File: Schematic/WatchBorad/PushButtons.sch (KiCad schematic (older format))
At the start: 16 parts, among them SW5 SW_Push, SW6 SW_Push, SW7 SW_Push, SW8 SW_Push, SW9 SW_Push, U6 max16054azt+t

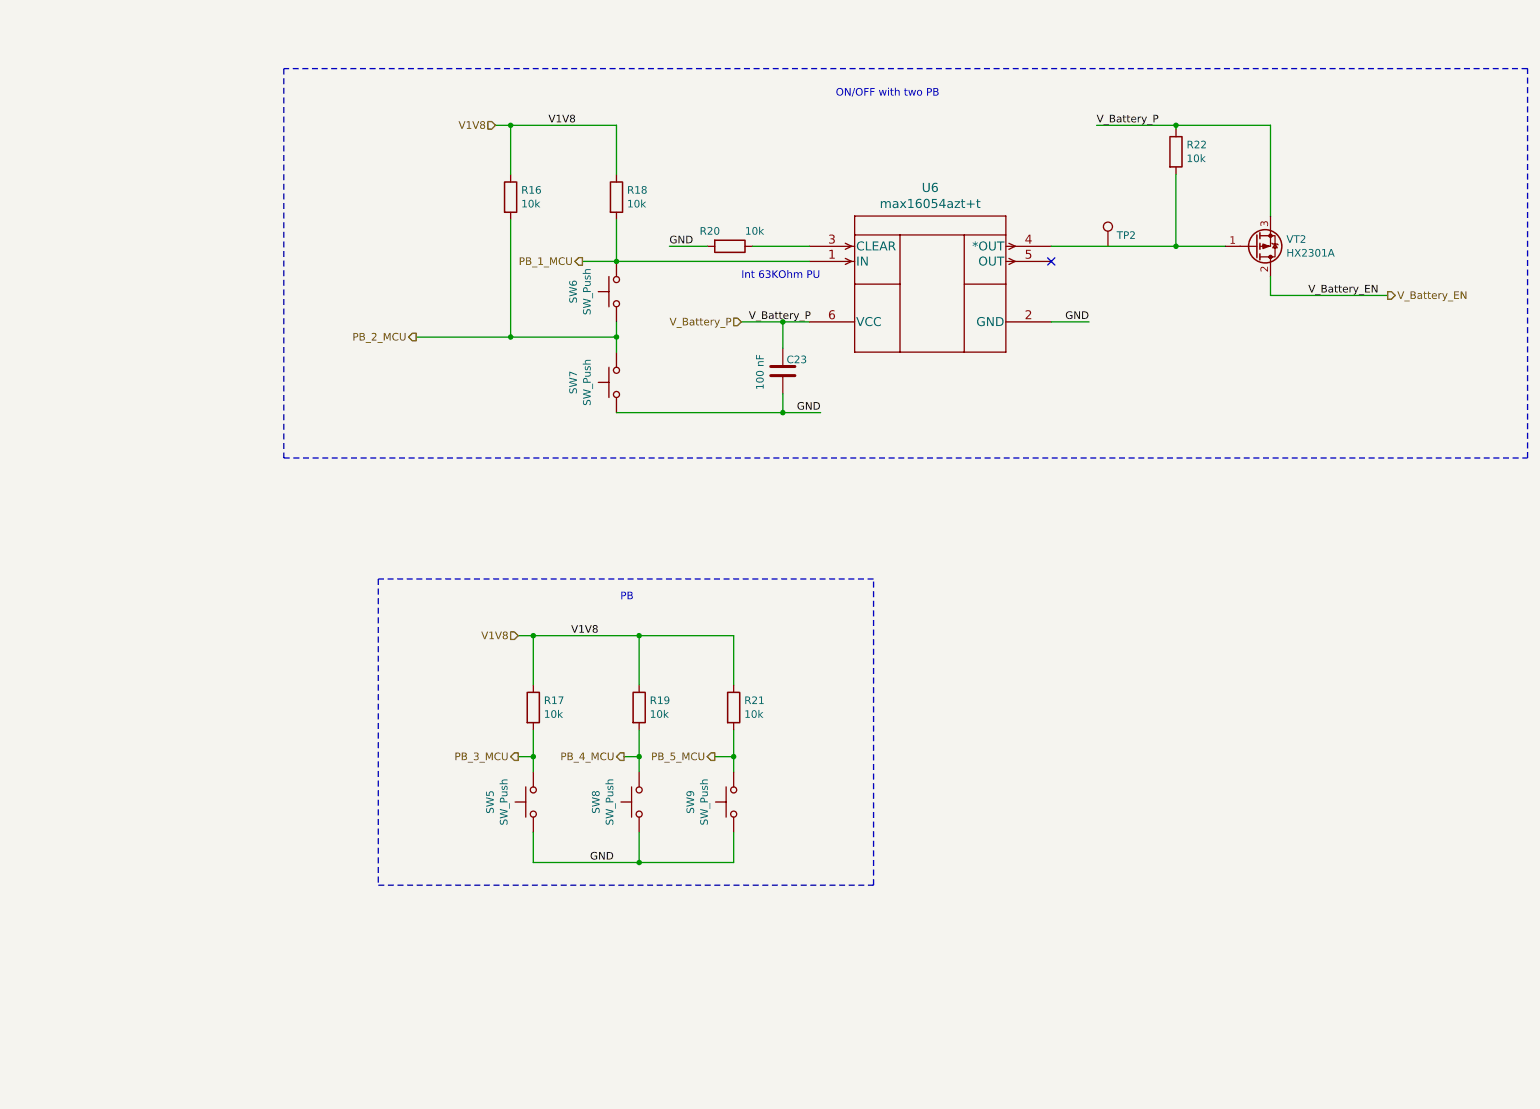
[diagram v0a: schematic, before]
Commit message: Display is replaced, now it has single power supply. One PSU is removed. Circuit PB is modified.
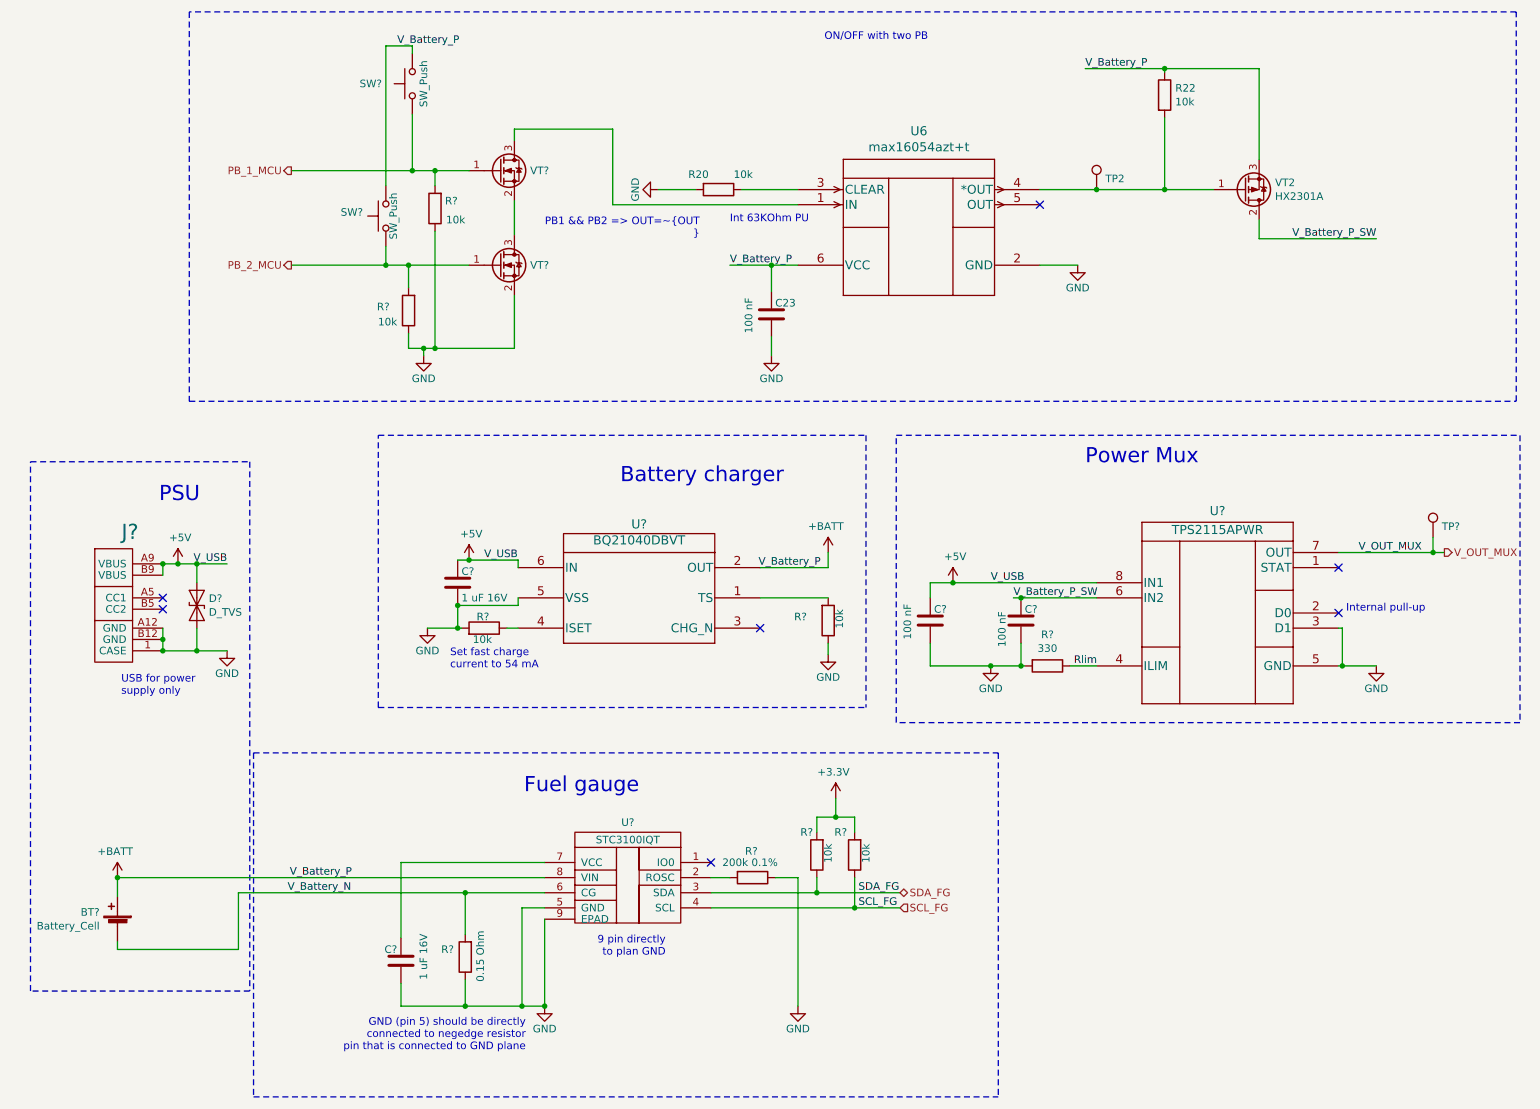
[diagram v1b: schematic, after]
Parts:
- removed R16, R17, R18, R19, R21: 10k, Resistors_SMD:R_0603_HandSoldering, symbol Device:R
- removed SW5, SW6, SW7, SW8, SW9: SW_Push, symbol Switch:SW_Push
- added BT?: Battery_Cell, symbol Device:Battery_Cell
- added C? (x2): 1 uF 16V, Capacitors_SMD:C_0603_HandSoldering, symbol Device:C
- added C? (x2): 100 nF, Capacitors_SMD:C_0603_HandSoldering, symbol Device:C
- added D?: D_TVS, symbol Device:D_TVS
- added J?: TYPE-C-31-M-17, symbol USB_connectors:TYPE-C-31-M-17
- added R? (x6): 10k, Resistors_SMD:R_0603_HandSoldering, symbol Device:R
- added R?: 200k 0.1%, Resistors_SMD:R_0603_HandSoldering, symbol Device:R
- added R?: 0.15 Ohm, Resistors_SMD:R_0603_HandSoldering, symbol Device:R
- added R?: 330, Resistors_SMD:R_0603_HandSoldering, symbol Device:R
- added SW? (x2): SW_Push, symbol Switch:SW_Push
- added TP?: TestPoint, testpoints:testpoint, symbol Connector:TestPoint
- added U?: BQ21040DBVT, TO_SOT_Packages_SMD:SOT-23-6, symbol BatteryManagmentLocal:BQ21040DBVT
- added U?: STC3100IQT, Housings_DFN_QFN:DFN-8-1EP_3x3mm_Pitch0.5mm, symbol BatteryManagmentLocal:STC3100IQT
- added U?: TPS2115APWR, Housings_SSOP:TSSOP-8_4.4x3mm_Pitch0.65mm, symbol PowerMuxes:TPS2115APWR
- added VT? (x2): SL2300, TO_SOT_Packages_SMD:SOT-23, symbol MosfetLocal:SL2300
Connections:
- net GND: now also C?.2, C?.2, C?.2, C?.2, D?.2 (A2), J?.1 (CASE), J?.A12 (GND), J?.B12 (GND), R?.1, R?.1, R?.1, R?.1, R?.1, R?.2, R?.2, U?.3 (D1), U?.5 (GND), U?.5 (GND), U?.5 (VSS), U?.9 (EPAD), VT?.2 (S)
- net PB_1_MCU: now also R?.2, SW?.1, VT?.1 (G); no longer U6.1 (IN)
- net PB_2_MCU: now also R?.2, SW?.1, VT?.1 (G)
- net at R22.2, U6.4 (*OUT), VT2.1 (G): now also TP2.1
- net V_Battery_EN renamed V_Battery_P_SW
- net V_Battery_P_SW: now also C?.1, U?.6 (IN2)
- net V_Battery_P renamed +BATT
- net +BATT: now also BT?.1 (+), SW?.2, SW?.2, U?.2 (OUT), U?.8 (VIN)
- new net: U6.1 (IN), VT?.3 (D)
- new net: R?.2, U?.1 (TS)
- new net: R?.1, U?.4 (ISET)
- new net: R?.2, U?.2 (ROSC)
- new net: C?.1, U?.7 (VCC)
- new net: VT?.2 (S), VT?.3 (D)
- new net +3V3: R?.2, R?.2
- new net +5V: C?.1, C?.1, D?.1 (A1), J?.A9 (VBUS), J?.B9 (VBUS), U?.6 (IN), U?.8 (IN1)
- new net Rlim: R?.1, U?.4 (ILIM)
- new net SCL_FG: R?.1, U?.4 (SCL)
- new net SDA_FG: R?.1, U?.3 (SDA)
- new net V_Battery_N: BT?.2 (-), R?.2, U?.6 (CG)
- new net V_OUT_MUX: TP?.1, U?.7 (OUT)
- no-connect marks 1 -> 7
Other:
- note added: "9 pin directly \nto plan GND\n"
- note added: "Battery charger\n"
- note added: "Fuel gauge"
- note added: "GND (pin 5) should be directly \nconnected to negedge resistor\npin that is connected to GND plane"
- note added: "Internal pull-up\n"
- note added: "PB1 && PB2 => OUT=~OUT\n"
- note added: "PSU"
- note added: "Power Mux\n"
- note added: "Set fast charge\ncurrent to 54 mA"
- note added: "USB for power \nsupply only\n"
- note removed: "PB\n"
- moved on the sheet: C23, R20, R22, TP2, U6, VT2
